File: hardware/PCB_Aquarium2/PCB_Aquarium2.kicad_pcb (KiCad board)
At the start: 4 copper layers, 71 x 61 mm, 104 parts, among them J1 Conn_01x03, J10 Conn_01x03, J11 Conn_01x03, J12 Conn_01x03, J13 Conn_01x03, J14 Conn_01x03, J15 Conn_01x03, J16 Conn_01x03, J17 Conn_01x03, J18 Conn_01x03, J19 Conn_01x03, J2 Conn_01x06, J20 Conn_01x02, J21 Conn_01x02, J22 Conn_01x02, J23 Conn_01x02, J24 Conn_01x03, J25 Conn_01x03, J26 Conn_01x03, J27 Conn_01x03, J28 Conn_01x03, J29 Conn_01x03, J3 Conn_01x02, J30 Conn_01x03, J31 Conn_01x03, J32 Conn_01x02, J33 Conn_01x02, J34 Conn_01x04, J35 Conn_ST_STDC14, J36 Conn_01x03, J37 Conn_01x03, J38 Conn_01x04, J4 Conn_01x02, J5 Conn_01x02, J6 Conn_01x06, J7 Conn_01x06, J8 Conn_01x03, J9 Conn_01x03, Q1 NMOS, Q2 NMOS, SW1 SW_SPST, SW2 SW_SPDT, U1 STM32G474RETx, U2 173010578, U3 AZ1117-3.3

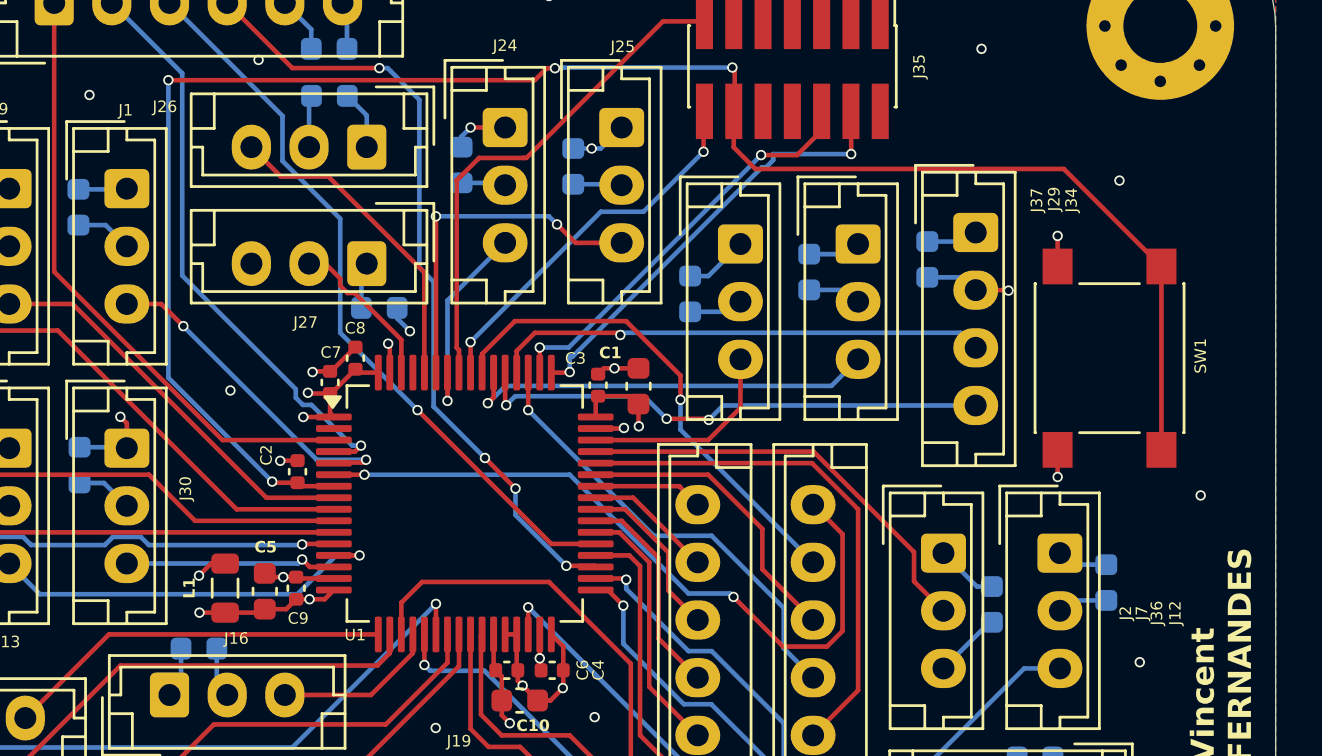
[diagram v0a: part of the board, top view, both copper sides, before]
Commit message: ajout des BOM
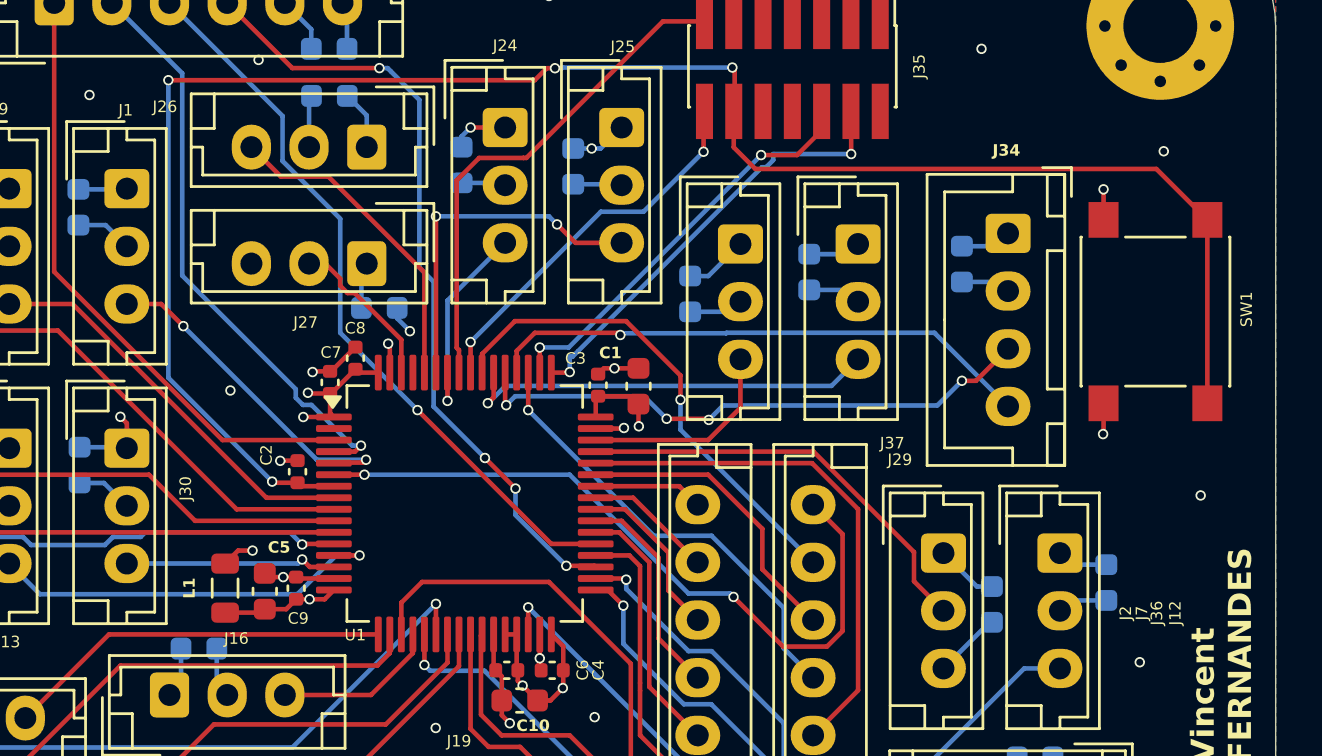
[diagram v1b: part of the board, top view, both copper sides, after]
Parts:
- J34: footprint Connector_JST:JST_EH_B4B-EH-A_1x04_P2.50mm_Vertical -> Connector_JST:JST_XH_B4B-XH-A_1x04_P2.50mm_Vertical
- moved SW1 2.84 mm to (180.8, 90.4)
- moved C41 1.51 mm to (172.4, 88.3)
- moved J34 1.40 mm to (174.4, 87.0)
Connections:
- J34 pad 3: USART3_TX -> USART3_RX
- J34 pad 4: USART3_RX -> USART3_TX
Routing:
- net USART3_TX: track 21.5 -> 24.0 mm
- net USART3_RX: track 22.6 -> 25.1 mm, vias 3 -> 4
- net GND: track 109.3 -> 107.9 mm, vias 51 -> 50
- net NRST: track 78.8 -> 80.0 mm
- net +3.3V: track 45.4 -> 44.4 mm, vias 11 -> 10
